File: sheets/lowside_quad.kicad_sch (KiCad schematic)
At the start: 4 parts, among them U1001 VNLD5090, U1002 VNLD5090

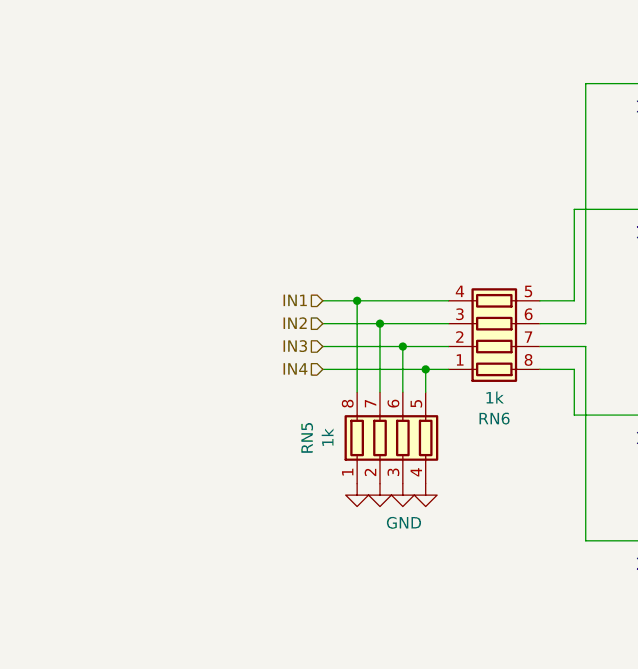
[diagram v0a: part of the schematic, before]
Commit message: Complete FOMEMC-11, FOMEMC-12, and FOMEMC-16: sync 492 PCB footprints, restore min_resolved_spokes=2 (0 starved thermals), enable teardrops, enforce >=1.2mm IGBT collector clearance, widen /IGN1..4_COIL, add WBO heater copper zones, and refresh CPL/BOM/renders
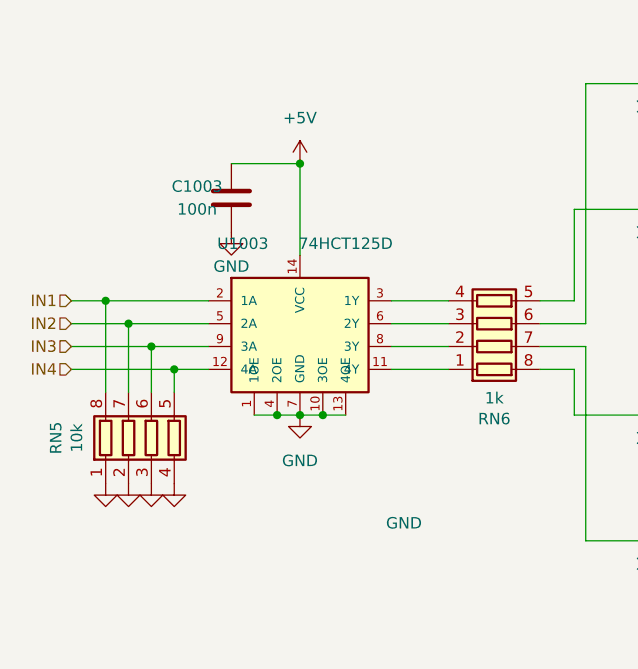
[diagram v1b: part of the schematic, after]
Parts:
- added C1003: 100n, Capacitor_SMD:C_0603_1608Metric, symbol Device:C
- added U1003: 74HCT125D, Package_SO:SOIC-14_3.9x8.7mm_P1.27mm, symbol 74xx:74HCT125D
- RN5: value 1k -> 10k; LCSC C20197 -> C29718; PN (none) -> 4D03WGJ0103T5E
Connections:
- net GND: now also C1003.2, U1003.1 (1OE), U1003.10 (3OE), U1003.13 (4OE), U1003.4 (2OE), U1003.7 (GND)
- net IN1: now also U1003.2 (1A); no longer RN6.4 (R4.1)
- net IN2: now also U1003.5 (2A); no longer RN6.3 (R3.1)
- net IN3: now also U1003.9 (3A); no longer RN6.2 (R2.1)
- net IN4: now also U1003.12 (4A); no longer RN6.1 (R1.1)
- new net: RN6.1 (R1.1), U1003.11 (4Y)
- new net: RN6.2 (R2.1), U1003.8 (3Y)
- new net: RN6.3 (R3.1), U1003.6 (2Y)
- new net: RN6.4 (R4.1), U1003.3 (1Y)
- new net +5V: C1003.1, U1003.14 (VCC)
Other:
- moved on the sheet: RN5

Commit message: Remediate FOMEMC-22..27: sheet contracts, doc/BOM/netlist parity, 494-part BOM/CPL, Mode A2 VR + C38/C39, wide WBO heater buses, and 4x M4 holes with 0 DRC warnings
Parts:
- C1003: LCSC C14663 -> C161115
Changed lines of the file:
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@@
 			(effects (font (size 1.27 1.27)) (hide yes))
 		)
-		(property "LCSC" "C14663"
+		(property "LCSC" "C161115"
 			(at 48.26 55.88 0)
 			(effects (font (size 1.27 1.27)) (hide yes))
